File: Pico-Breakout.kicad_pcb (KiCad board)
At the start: 2 copper layers, 38.1 x 52.1 mm, 3 parts, among them J101 Conn_01x20, J102 Conn_01x20, U101 Pico

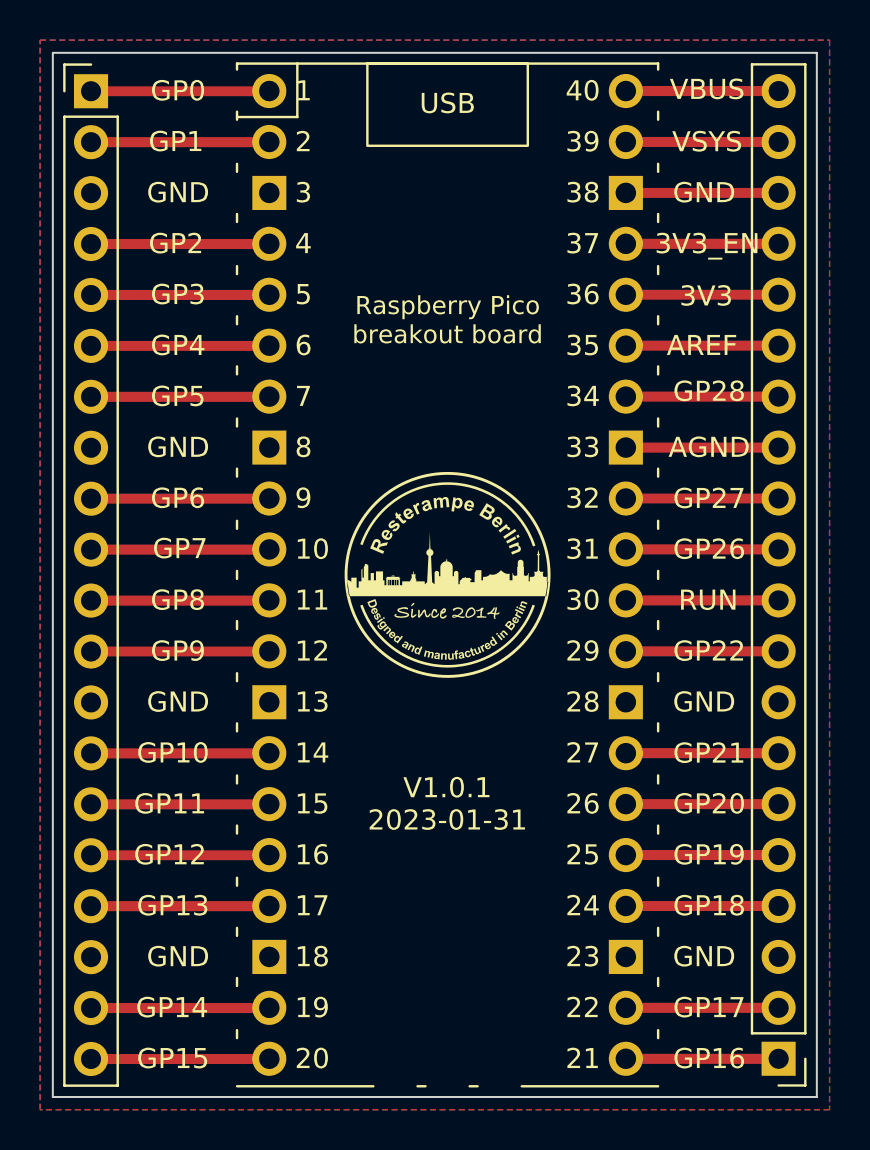
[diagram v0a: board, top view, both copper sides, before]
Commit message: Added 3D stacking header
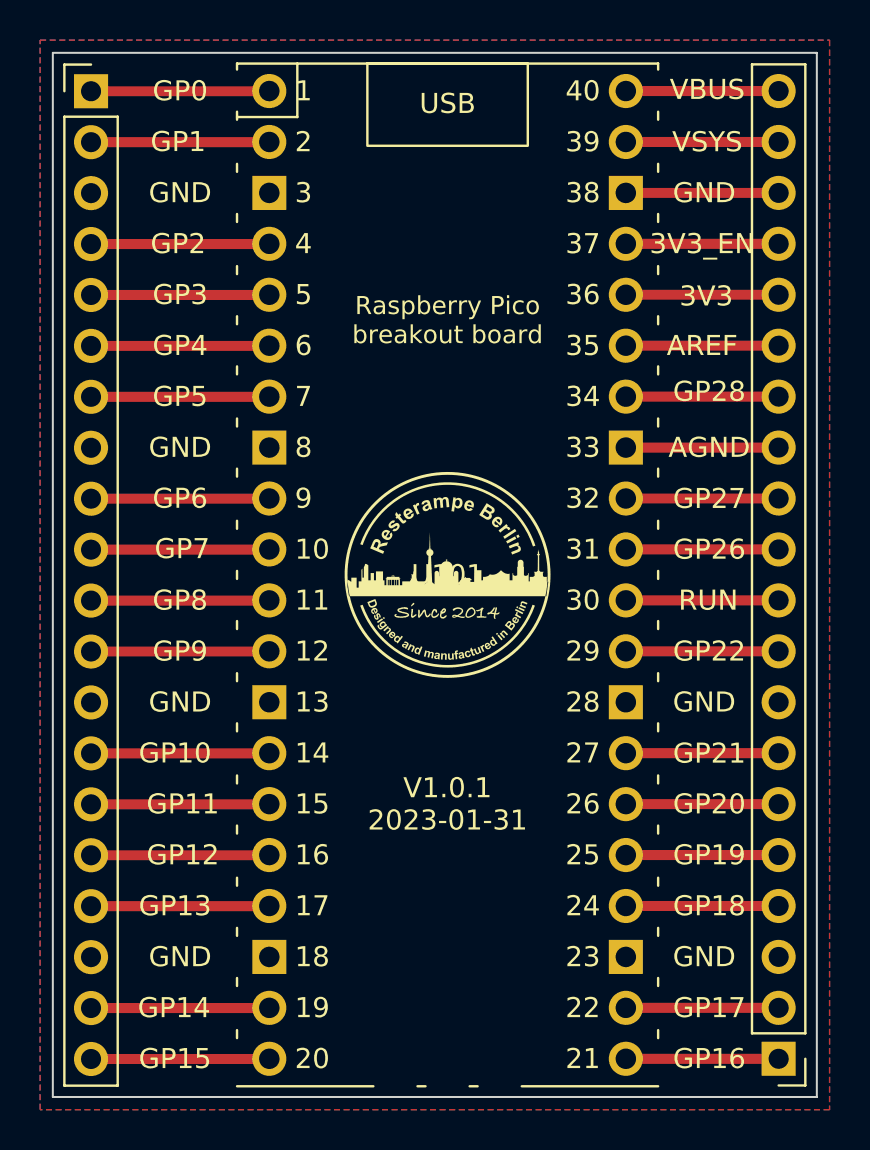
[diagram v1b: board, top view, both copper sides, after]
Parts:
- U101: footprint MCU_RaspberryPi_and_Boards:RPi_Pico_TH -> Pico:RPi_Pico_Stacking_TH

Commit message: Names streamlined
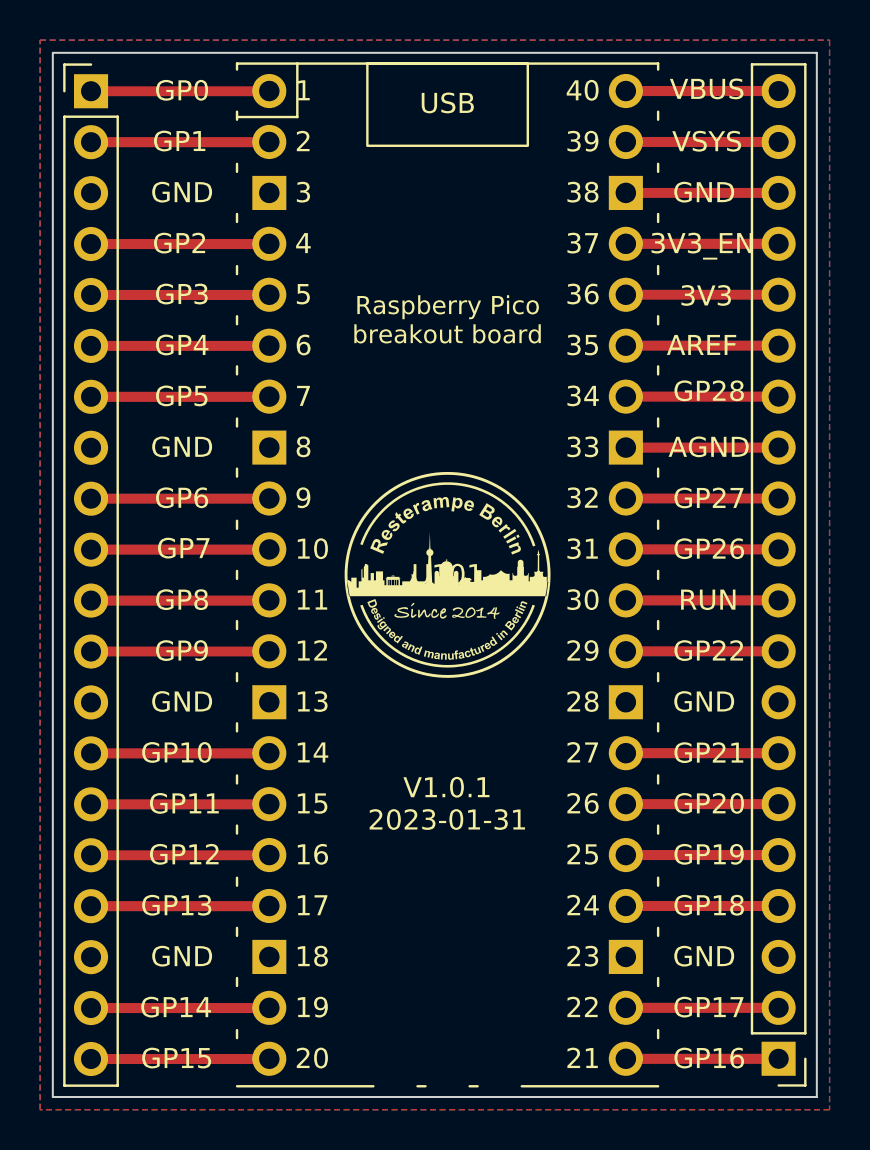
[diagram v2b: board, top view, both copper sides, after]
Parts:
- U101: footprint Pico:RPi_Pico_Stacking_TH -> Pico:RPi_Pico_Stacking_header_TH
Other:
- board text added: "3V3"
- board text added: "3V3_EN"
- board text added: "AGND"
- board text added: "AREF"
- board text added: "GND"
- board text added: "GP0"
- board text added: "GP1"
- board text added: "GP10"
- board text added: "GP11"
- board text added: "GP12"
- board text added: "GP13"
- board text added: "GP14"
- board text added: "GP15"
- board text added: "GP16"
- board text added: "GP17"
- board text added: "GP18"
- board text added: "GP19"
- board text added: "GP2"
- board text added: "GP20"
- board text added: "GP21"
- board text added: "GP22"
- board text added: "GP26"
- board text added: "GP27"
- board text added: "GP28"
- board text added: "GP3"
- board text added: "GP4"
- board text added: "GP5"
- board text added: "GP6"
- board text added: "GP7"
- board text added: "GP8"
- board text added: "GP9"
- board text added: "RUN"
- board text added: "VBUS"
- board text added: "VSYS"
